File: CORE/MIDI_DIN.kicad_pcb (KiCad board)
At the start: 2 copper layers, 29.5 x 99.8 mm, 60 parts, among them J1 Conn_02x08_Odd_Even, J2 USB_C_Receptacle_USB2.0, J3 Conn_01x04, J5 MAB5100S, J6 MAB5100S, J7 Conn_01x06, Q1 MMBT3906, SW1 SW_SPDT, SW2 SW_Push_DPDT, SW3 PROG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

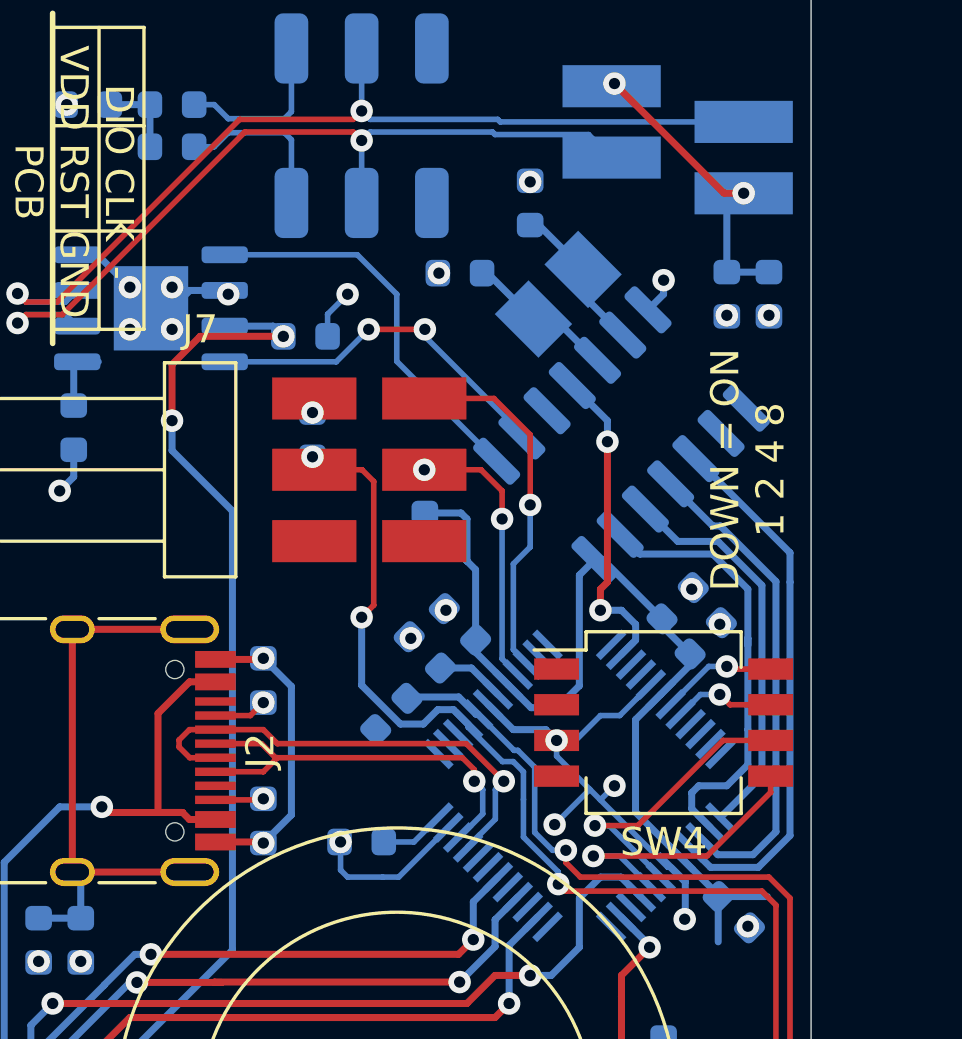
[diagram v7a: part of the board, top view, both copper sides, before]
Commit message: Make room for latching connector
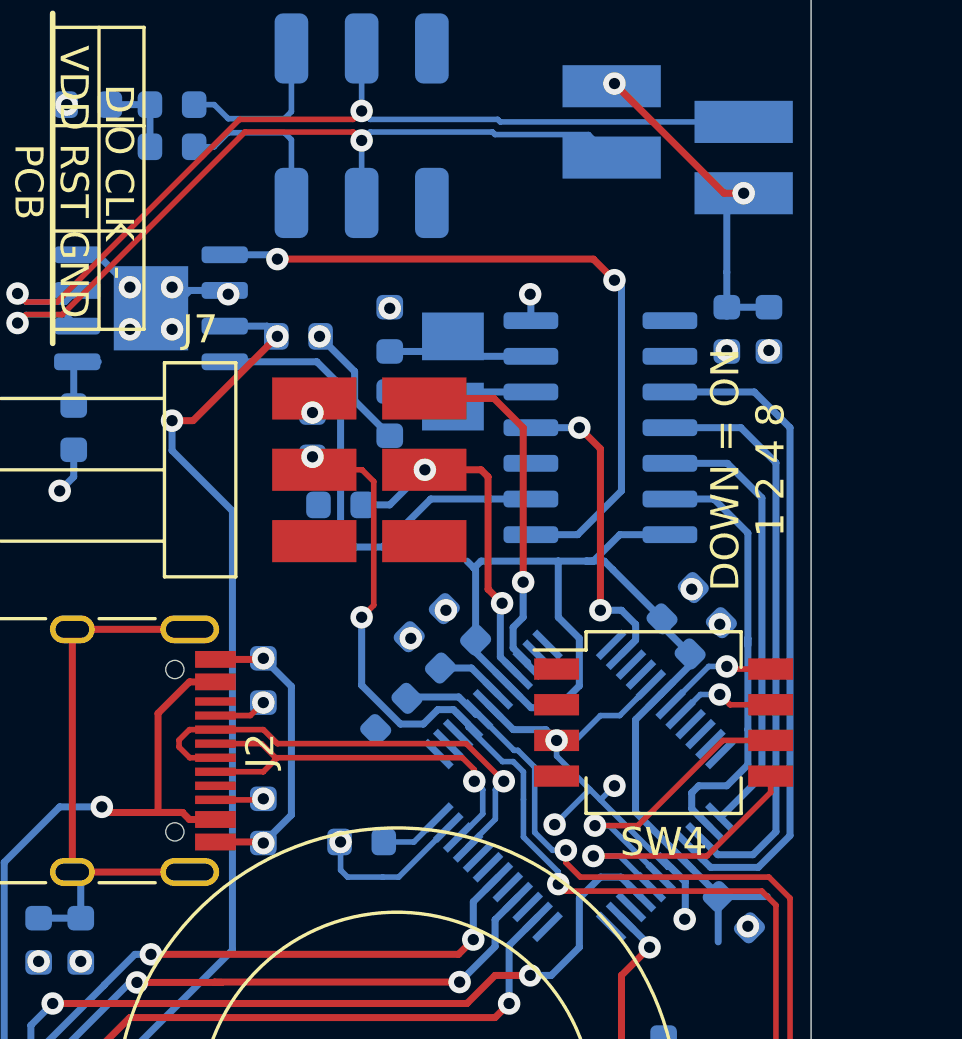
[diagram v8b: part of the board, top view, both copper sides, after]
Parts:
- J3: footprint Custom_FP:MicroMatch_04_Vertical_SMD -> Custom_FP:MicroMatch_04_Vertical_SMD_Lock
- moved C14 6.73 mm to (89.8, 57.8)
- moved C13 5.59 mm to (89.8, 60.8), turned to 270 degrees
- moved Y1 4.65 mm to (92.0, 59.2), turned to 90 degrees
- moved R15 3.04 mm to (88.0, 64.0), turned to 0 degrees
- moved C12 1.25 mm to (103.2, 57.8)
- moved R21 1.25 mm to (101.8, 57.8)
- moved U4 0.79 mm to (97.2, 61.2), turned to 0 degrees
- moved C11 0.25 mm to (86.5, 58.0)
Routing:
- net Net-(U4-Pad1): track 14.1 -> 25.7 mm, vias 0 -> 2
- net Net-(U4-Pad2): track 12.8 -> 17.4 mm, vias 2 -> 0
- net SPI_SCK: track 19.1 -> 23.6 mm
- net +3V3: track 44.3 -> 48.4 mm
- net SPI_MOSI: track 17.4 -> 20.7 mm
- net SWCLK: track 9.90 -> 12.6 mm
- net GND: track 45.7 -> 48.2 mm, vias 56 -> 55
- net SPI_MISO: track 14.2 -> 15.8 mm
- net +5V: track 72.1 -> 70.6 mm
- net Net-(C12-Pad1): track 10.9 -> 12.2 mm
- net Net-(C13-Pad1): track 6.16 -> 5.46 mm
